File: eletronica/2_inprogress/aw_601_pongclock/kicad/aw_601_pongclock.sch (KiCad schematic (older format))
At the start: 89 parts, among them IC1 ATMEGA8-P, Q1 2N3904G, Q10 2N3904G, Q11 2N3904G, Q12 2N3904G, Q13 2N3904G, Q14 2N3904G, Q15 2N3904G, Q16 2N3904G, Q17 2N3904G, Q18 2N3904G, Q19 2N3904G, Q2 2N3904G, Q20 2N3904G, Q21 2N3904G, Q22 2N3904G, Q23 2N3904G, Q24 2N3904G, Q25 2N3904G, Q26 2N3904G, Q27 2N3904G, Q28 2N3904G, Q29 2N3904G, Q3 2N3904G, Q30 2N3904G, Q31 2N3904G, Q32 2N3904G, Q4 2N3904G, Q5 2N3904G, Q6 2N3904G, Q7 2N3904G, Q8 2N3904G, Q9 2N3904G, SW1 SW_PUSH, SW2 SW_PUSH, SW3 SW_PUSH, SW4 SW_PUSH, U1 4514, U2 ULN2803, U3 ULN2803, U4 ULN2803, U5 ULN2803, U6 74HC4094, U7 74HC4094, U8 74HC4094, U9 74HC4094, X1 16Mhz

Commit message: 
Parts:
- added CON?: BARREL_JACK, symbol BARREL_JACK
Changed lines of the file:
@@
-EESchema Schematic File Version 2  date 13/06/2013 09:27:16
+EESchema Schematic File Version 2  date 13/06/2013 16:50:11
 LIBS:power
 LIBS:device
@@
 Text Label 3400 3700 0    60   ~ 0
 STRB
+$Comp
+L BARREL_JACK CON?
+U 1 1 51BA212D
+P 5250 1250
+F 0 "CON?" H 5250 1500 60  0000 C CNN
+F 1 "BARREL_JACK" H 5250 1050 60  0000 C CNN
+F 2 "" H 5250 1250 60  0000 C CNN
+F 3 "" H 5250 1250 60  0000 C CNN
+	1    5250 1250
+	1    0    0    -1
+$EndComp
 $EndSCHEMATC

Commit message: 
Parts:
- added C3: CP1, ~, symbol CP1
- gave numbers to parts that had none: 1
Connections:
- wire segments 362 -> 370
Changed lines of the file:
@@
-EESchema Schematic File Version 2  date 13/06/2013 16:50:11
+EESchema Schematic File Version 2  date 14/06/2013 09:56:47
 LIBS:power
 LIBS:device
@@
 Sheet 1 1
 Title "AW601 Pong Clock"
-Date "13 jun 2013"
+Date "14 jun 2013"
 Rev ""
 Comp "Imperial Electronics"
@@
 Text Label 8700 1950 0    60   ~ 0
 V3
-Text Label 8700 2050 0    60   ~ 0
-V4
-Text Label 8700 2150 0    60   ~ 0
-V5
-Text Label 8700 2250 0    60   ~ 0
-V6
-Text Label 8700 2350 0    60   ~ 0
-V7
-Text Label 8700 2450 0    60   ~ 0
-V8
 Text Label 8750 3850 0    60   ~ 0
 V9
@@
 Text Label 11800 4050 0    60   ~ 0
 V27
-Text Label 11800 4150 0    60   ~ 0
-V28
-Text Label 11800 4250 0    60   ~ 0
-V29
-Text Label 11800 4350 0    60   ~ 0
-V30
-Text Label 11800 4450 0    60   ~ 0
-V31
-Text Label 11800 4550 0    60   ~ 0
-V32
 Entry Wire Line
 	6000 5350 6100 5250
@@
 Text Label 6600 5350 1    60   ~ 0
 V3
-Text Label 6800 5350 1    60   ~ 0
-V4
-Text Label 7200 5350 1    60   ~ 0
-V5
-Text Label 7400 5350 1    60   ~ 0
-V6
-Text Label 7800 5350 1    60   ~ 0
-V7
-Text Label 8000 5350 1    60   ~ 0
-V8
 Text Label 8400 5350 1    60   ~ 0
 V9
@@
 Text Label 13900 5350 1    60   ~ 0
 V27
-Text Label 14100 5350 1    60   ~ 0
-V28
-Text Label 14500 5350 1    60   ~ 0
-V29
-Text Label 14700 5350 1    60   ~ 0
-V30
-Text Label 15100 5350 1    60   ~ 0
-V31
-Text Label 15300 5350 1    60   ~ 0
-V32
 $Comp
 L SW_PUSH SW1
@@
 L +5V #PWR08
 U 1 1 51B19F4D
-P 2350 1600
-F 0 "#PWR08" H 2350 1690 20  0001 C CNN
-F 1 "+5V" H 2350 1690 30  0000 C CNN
-F 2 "" H 2350 1600 60  0000 C CNN
-F 3 "" H 2350 1600 60  0000 C CNN
-	1    2350 1600
+P 2350 1000
+F 0 "#PWR08" H 2350 1090 20  0001 C CNN
+F 1 "+5V" H 2350 1090 30  0000 C CNN
+F 2 "" H 2350 1000 60  0000 C CNN
+F 3 "" H 2350 1000 60  0000 C CNN
+	1    2350 1000
 	1    0    0    -1
 $EndComp
@@
 STRB
 $Comp
-L BARREL_JACK CON?
+L BARREL_JACK CON1
 U 1 1 51BA212D
 P 5250 1250
-F 0 "CON?" H 5250 1500 60  0000 C CNN
+F 0 "CON1" H 5250 1500 60  0000 C CNN
 F 1 "BARREL_JACK" H 5250 1050 60  0000 C CNN
 F 2 "" H 5250 1250 60  0000 C CNN
@@
 	1    0    0    -1
 $EndComp
+$Comp
+L +5V #PWR014
+U 1 1 51BAFAF5
+P 5600 1050
+F 0 "#PWR014" H 5600 1140 20  0001 C CNN
+F 1 "+5V" H 5600 1140 30  0000 C CNN
+F 2 "" H 5600 1050 60  0000 C CNN
+F 3 "" H 5600 1050 60  0000 C CNN
+	1    5600 1050
+	1    0    0    -1
+$EndComp
+$Comp
+L GND #PWR015
+U 1 1 51BAFAFB
+P 5600 1450
+F 0 "#PWR015" H 5600 1450 30  0001 C CNN
+F 1 "GND" H 5600 1380 30  0001 C CNN
+F 2 "" H 5600 1450 60  0000 C CNN
+F 3 "" H 5600 1450 60  0000 C CNN
+	1    5600 1450
+	1    0    0    -1
+$EndComp
+Wire Wire Line
+	5550 1150 5600 1150
+Wire Wire Line
+	5600 1150 5600 1050
+Wire Wire Line
+	5550 1250 5600 1250
+Wire Wire Line
+	5600 1250 5600 1450
+Wire Wire Line
+	5550 1350 5600 1350
+Connection ~ 5600 1350
+Wire Wire Line
+	2350 1000 2350 1600
+$Comp
+L CP1 C3
+U 1 1 51BB0678
+P 2050 1300
+F 0 "C3" H 2100 1400 50  0000 L CNN
+F 1 "CP1" H 2100 1200 50  0000 L CNN
+F 2 "~" H 2050 1300 60  0000 C CNN
+F 3 "~" H 2050 1300 60  0000 C CNN
+	1    2050 1300
+	1    0    0    -1
+$EndComp
+$Comp
+L GND #PWR016
+U 1 1 51BB0685
+P 2050 1550
+F 0 "#PWR016" H 2050 1550 30  0001 C CNN
+F 1 "GND" H 2050 1480 30  0001 C CNN
+F 2 "" H 2050 1550 60  0000 C CNN
+F 3 "" H 2050 1550 60  0000 C CNN
+	1    2050 1550
+	1    0    0    -1
+$EndComp
+Wire Wire Line
+	2050 1100 2350 1100
+Connection ~ 2350 1100
+Wire Wire Line
+	2050 1500 2050 1550
+Text Label 8700 2050 0    60   ~ 0
+V4
+Text Label 8700 2150 0    60   ~ 0
+V5
+Text Label 8700 2250 0    60   ~ 0
+V6
+Text Label 8700 2350 0    60   ~ 0
+V7
+Text Label 8700 2450 0    60   ~ 0
+V8
+Text Label 6800 5350 1    60   ~ 0
+V4
+Text Label 7200 5350 1    60   ~ 0
+V5
+Text Label 7400 5350 1    60   ~ 0
+V6
+Text Label 7800 5350 1    60   ~ 0
+V7
+Text Label 8000 5350 1    60   ~ 0
+V8
+Text Label 8450 2050 0    60   ~ 0
+V4
+Text Label 6800 5500 0    60   ~ 0
+V4
+Text Label 11800 4150 0    60   ~ 0
+V28
+Text Label 11800 4250 0    60   ~ 0
+V29
+Text Label 11800 4350 0    60   ~ 0
+V30
+Text Label 11800 4450 0    60   ~ 0
+V31
+Text Label 11800 4550 0    60   ~ 0
+V32
+Text Label 14100 5350 1    60   ~ 0
+V28
+Text Label 14500 5350 1    60   ~ 0
+V29
+Text Label 14700 5350 1    60   ~ 0
+V30
+Text Label 15100 5350 1    60   ~ 0
+V31
+Text Label 15300 5350 1    60   ~ 0
+V32
 $EndSCHEMATC

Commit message: 
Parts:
- removed RV1, RV2, RV3: 2K, ~, symbol POT
- added BT1: BATTERY, ~, symbol BATTERY
- added R11: 10K, ~, symbol R
- added U10: DS1307, ~, symbol DS1307
- added X2: 16Mhz, ~, symbol CRYSTAL
- R1: value 680 -> 1.8K
- R2: value 680 -> 220
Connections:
- net labels added: BUTTONS, SCL, SDA
- wire segments 370 -> 366
- no-connect marks 14 -> 16
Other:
- moved on the sheet: R1, R2, R3, SW1, SW2, SW3, SW4

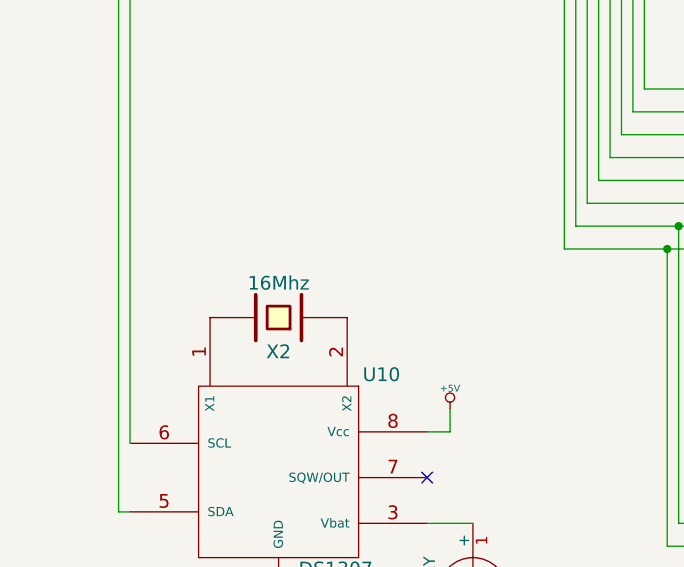
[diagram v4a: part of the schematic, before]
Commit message: 
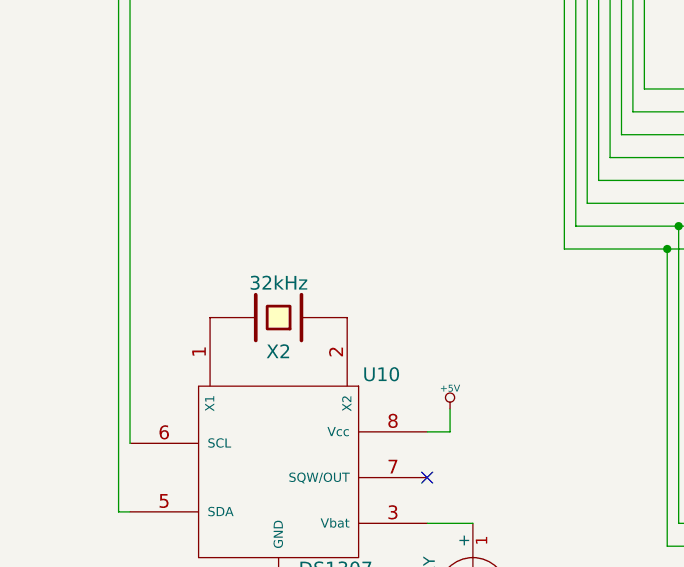
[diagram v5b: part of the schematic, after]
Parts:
- X2: value 16Mhz -> 32kHz
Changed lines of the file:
@@
 Sheet 1 1
 Title "AW601 Pong Clock"
-Date "28 jun 2013"
+Date "30 jun 2013"
 Rev ""
 Comp "Imperial Electronics"
@@
 P 1750 8800
 F 0 "X2" H 1750 8950 60  0000 C CNN
-F 1 "16Mhz" H 1750 8650 60  0000 C CNN
+F 1 "32kHz" H 1750 8650 60  0000 C CNN
 F 2 "~" H 1750 8800 60  0000 C CNN
 F 3 "~" H 1750 8800 60  0000 C CNN

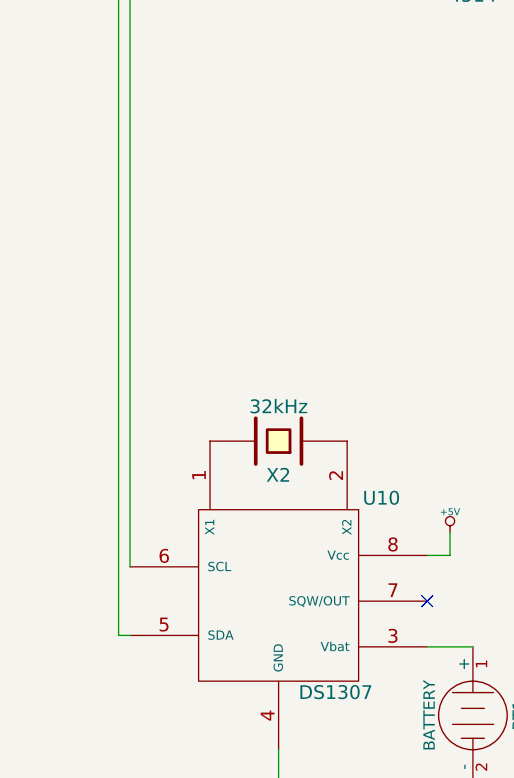
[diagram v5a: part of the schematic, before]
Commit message: 
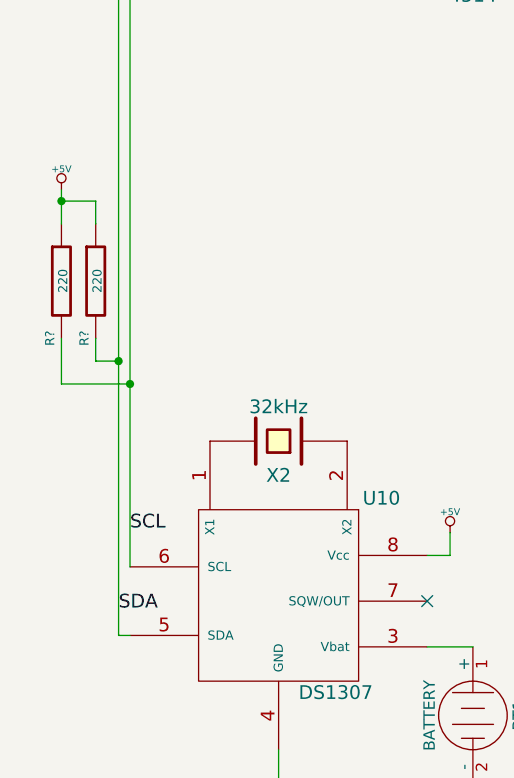
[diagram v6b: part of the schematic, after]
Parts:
- added R? (x2): 220, ~, symbol R
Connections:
- net +5V: now also R?.1, R?.1
- net SCL: now also IC1.12 ((AIN0)PD6), U10.6 (SCL), R?.2
- net SDA: now also R?.2
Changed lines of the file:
@@
 Sheet 1 1
 Title "AW601 Pong Clock"
-Date "30 jun 2013"
+Date "11 sep 2013"
 Rev ""
 Comp "Imperial Electronics"
@@
 Wire Wire Line
 	2600 9700 2400 9700
+Text Label 1050 9550 0    60   ~ 0
+SDA
+Text Label 1100 9200 0    60   ~ 0
+SCL
+$Comp
+L R R?
+U 1 1 5230ED52
+P 950 8100
+F 0 "R?" V 900 7850 40  0000 C CNN
+F 1 "220" V 957 8101 40  0000 C CNN
+F 2 "~" V 880 8100 30  0000 C CNN
+F 3 "~" H 950 8100 30  0000 C CNN
+	1    950  8100
+	1    0    0    -1
+$EndComp
+$Comp
+L R R?
+U 1 1 5230ED5F
+P 800 8100
+F 0 "R?" V 750 7850 40  0000 C CNN
+F 1 "220" V 807 8101 40  0000 C CNN
+F 2 "~" V 730 8100 30  0000 C CNN
+F 3 "~" H 800 8100 30  0000 C CNN
+	1    800  8100
+	1    0    0    -1
+$EndComp
+$Comp
+L +5V #PWR?
+U 1 1 5230ED71
+P 800 7700
+F 0 "#PWR?" H 800 7790 20  0001 C CNN
+F 1 "+5V" H 800 7790 30  0000 C CNN
+F 2 "" H 800 7700 60  0000 C CNN
+F 3 "" H 800 7700 60  0000 C CNN
+	1    800  7700
+	1    0    0    -1
+$EndComp
+Wire Wire Line
+	800  7850 800  7700
+Wire Wire Line
+	950  7850 950  7750
+Wire Wire Line
+	950  7750 800  7750
+Connection ~ 800  7750
+Wire Wire Line
+	950  8350 950  8450
+Wire Wire Line
+	950  8450 1050 8450
+Connection ~ 1050 8450
+Wire Wire Line
+	800  8350 800  8550
+Wire Wire Line
+	800  8550 1100 8550
+Connection ~ 1100 8550
 $EndSCHEMATC

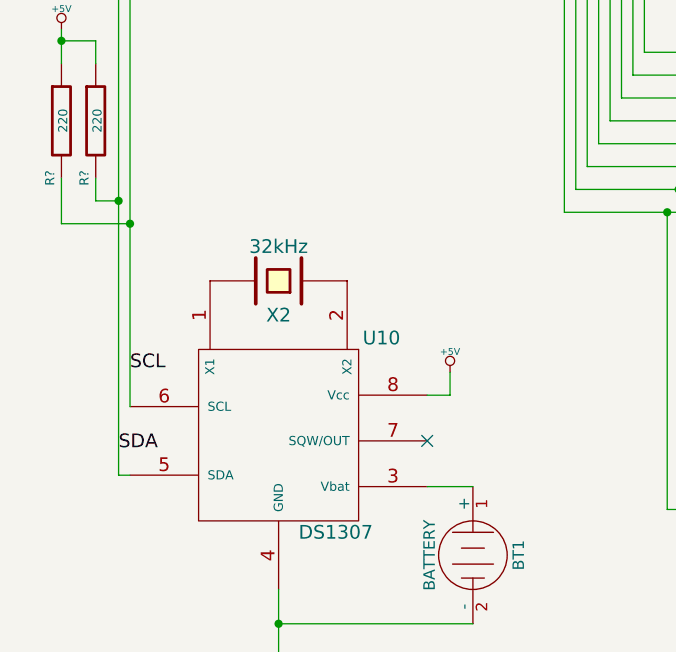
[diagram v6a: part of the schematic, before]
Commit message: 
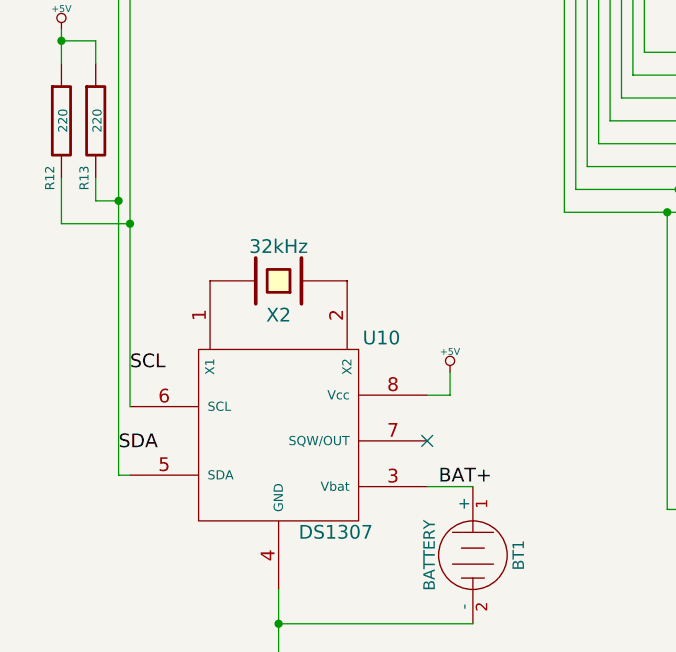
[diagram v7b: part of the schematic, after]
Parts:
- gave numbers to parts that had none: 2
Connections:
- net BAT+: now reaches BT1.1 (+), U10.3 (Vbat)
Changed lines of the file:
@@
-EESchema Schematic File Version 2
+EESchema Schematic File Version 2  date 13/09/2013 08:24:44
 LIBS:power
 LIBS:device
@@
 Sheet 1 1
 Title "AW601 Pong Clock"
-Date "11 sep 2013"
+Date "13 sep 2013"
 Rev ""
 Comp "Imperial Electronics"
@@
 SCL
 $Comp
-L R R?
+L R R13
 U 1 1 5230ED52
 P 950 8100
-F 0 "R?" V 900 7850 40  0000 C CNN
+F 0 "R13" V 900 7850 40  0000 C CNN
 F 1 "220" V 957 8101 40  0000 C CNN
 F 2 "~" V 880 8100 30  0000 C CNN
@@
 $EndComp
 $Comp
-L R R?
+L R R12
 U 1 1 5230ED5F
 P 800 8100
-F 0 "R?" V 750 7850 40  0000 C CNN
+F 0 "R12" V 750 7850 40  0000 C CNN
 F 1 "220" V 807 8101 40  0000 C CNN
 F 2 "~" V 730 8100 30  0000 C CNN
@@
 $EndComp
 $Comp
-L +5V #PWR?
+L +5V #PWR019
 U 1 1 5230ED71
 P 800 7700
-F 0 "#PWR?" H 800 7790 20  0001 C CNN
+F 0 "#PWR019" H 800 7790 20  0001 C CNN
 F 1 "+5V" H 800 7790 30  0000 C CNN
 F 2 "" H 800 7700 60  0000 C CNN
@@
 	800  8550 1100 8550
 Connection ~ 1100 8550
+Text Label 2450 9700 0    60   ~ 0
+BAT+
 $EndSCHEMATC

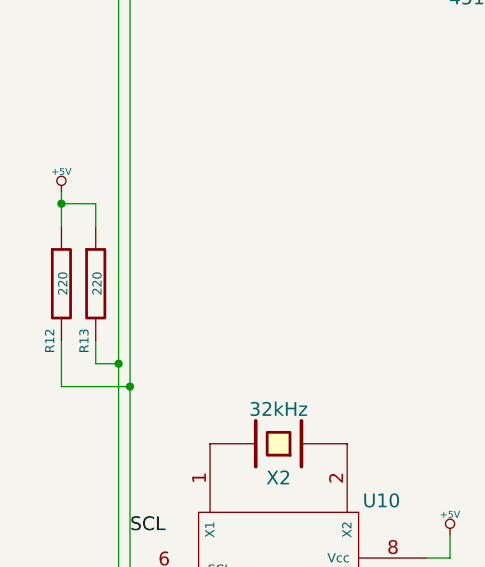
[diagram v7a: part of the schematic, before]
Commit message: 
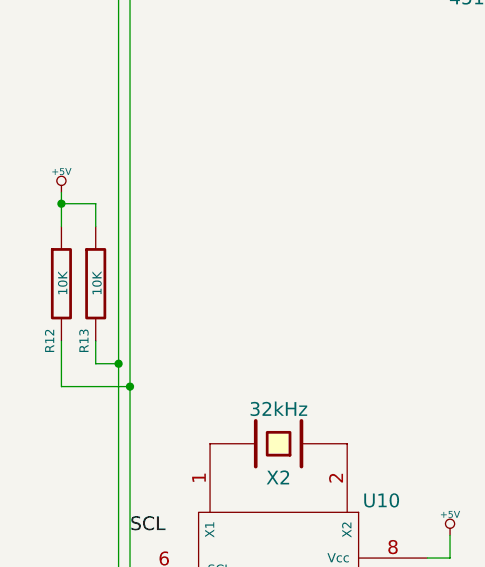
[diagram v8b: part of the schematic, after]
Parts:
- R12, R13: value 220 -> 10K
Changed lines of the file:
@@
-EESchema Schematic File Version 2  date 13/09/2013 08:24:44
+EESchema Schematic File Version 2
 LIBS:power
 LIBS:device
@@
 Sheet 1 1
 Title "AW601 Pong Clock"
-Date "13 sep 2013"
+Date "15 sep 2013"
 Rev ""
 Comp "Imperial Electronics"
@@
 P 950 8100
 F 0 "R13" V 900 7850 40  0000 C CNN
-F 1 "220" V 957 8101 40  0000 C CNN
+F 1 "10K" V 957 8101 40  0000 C CNN
 F 2 "~" V 880 8100 30  0000 C CNN
 F 3 "~" H 950 8100 30  0000 C CNN
@@
 P 800 8100
 F 0 "R12" V 750 7850 40  0000 C CNN
-F 1 "220" V 807 8101 40  0000 C CNN
+F 1 "10K" V 807 8101 40  0000 C CNN
 F 2 "~" V 730 8100 30  0000 C CNN
 F 3 "~" H 800 8100 30  0000 C CNN
